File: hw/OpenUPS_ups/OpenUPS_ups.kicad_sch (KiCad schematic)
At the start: 15 parts, among them J101 XT60PW-M, J102 Barrel Jack, J103 Screw Terminal, J104 Screw Terminal, J105 Screw Terminal, J106 JST XH, J107 JST XH, U102 AVR32DB48x-xPT

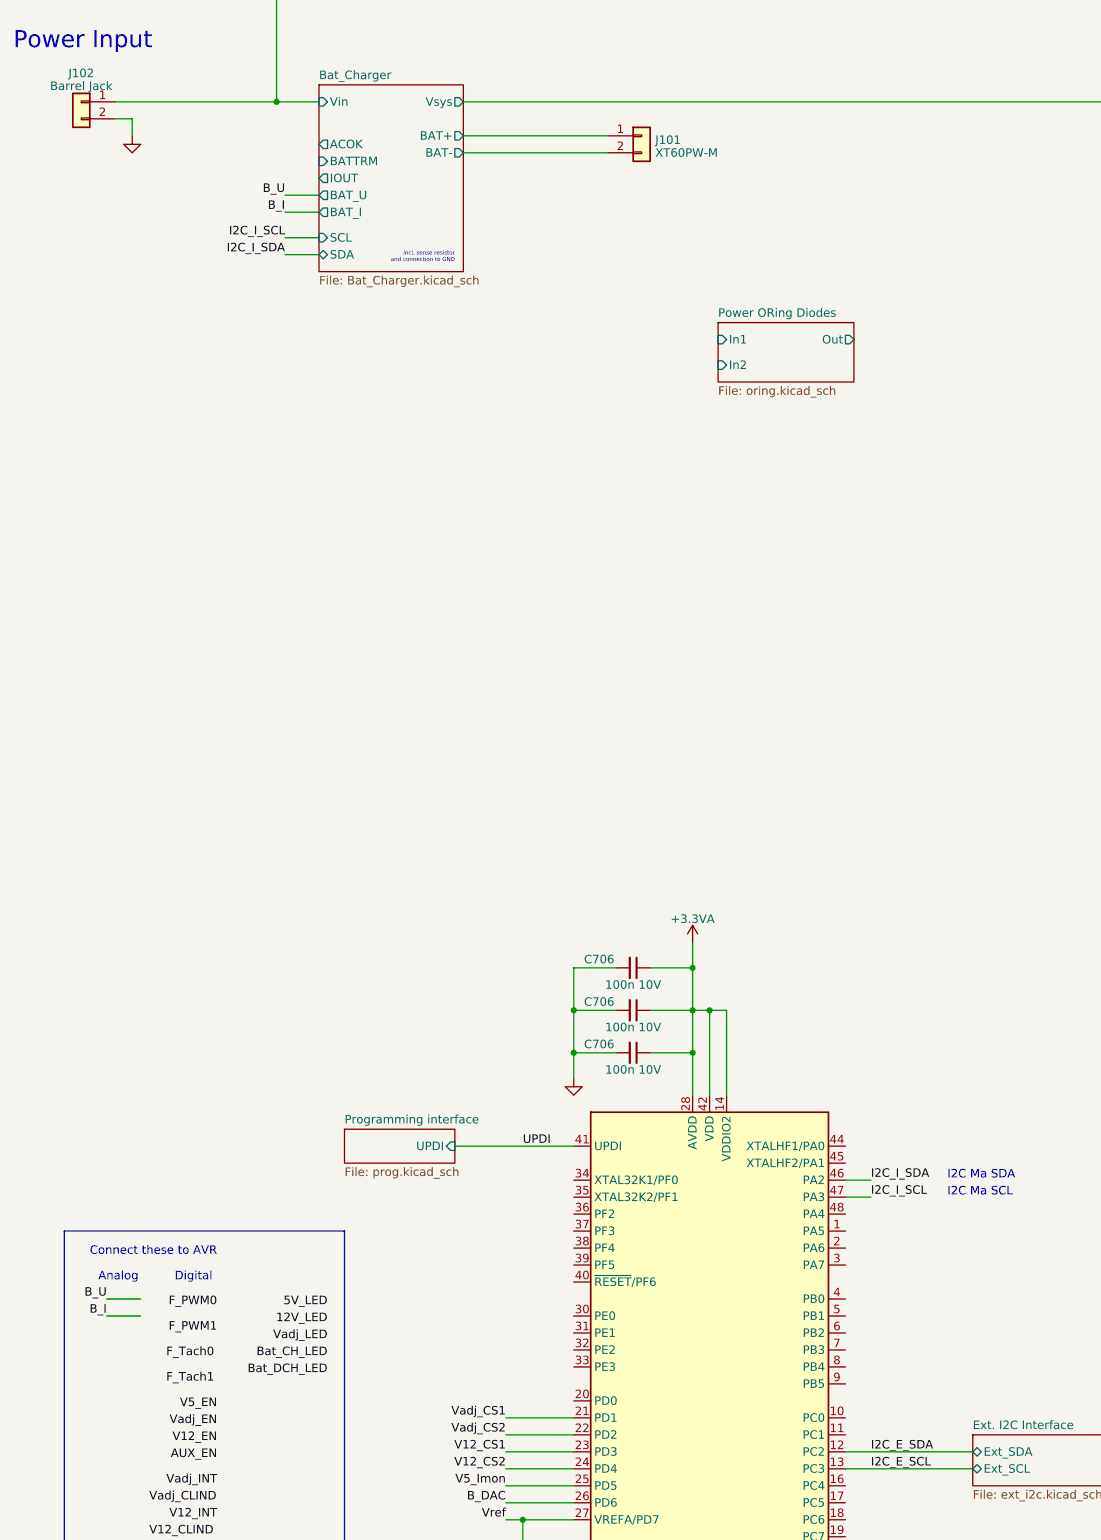
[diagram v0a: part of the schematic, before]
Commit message: Issue #24 - battery charger, good for review
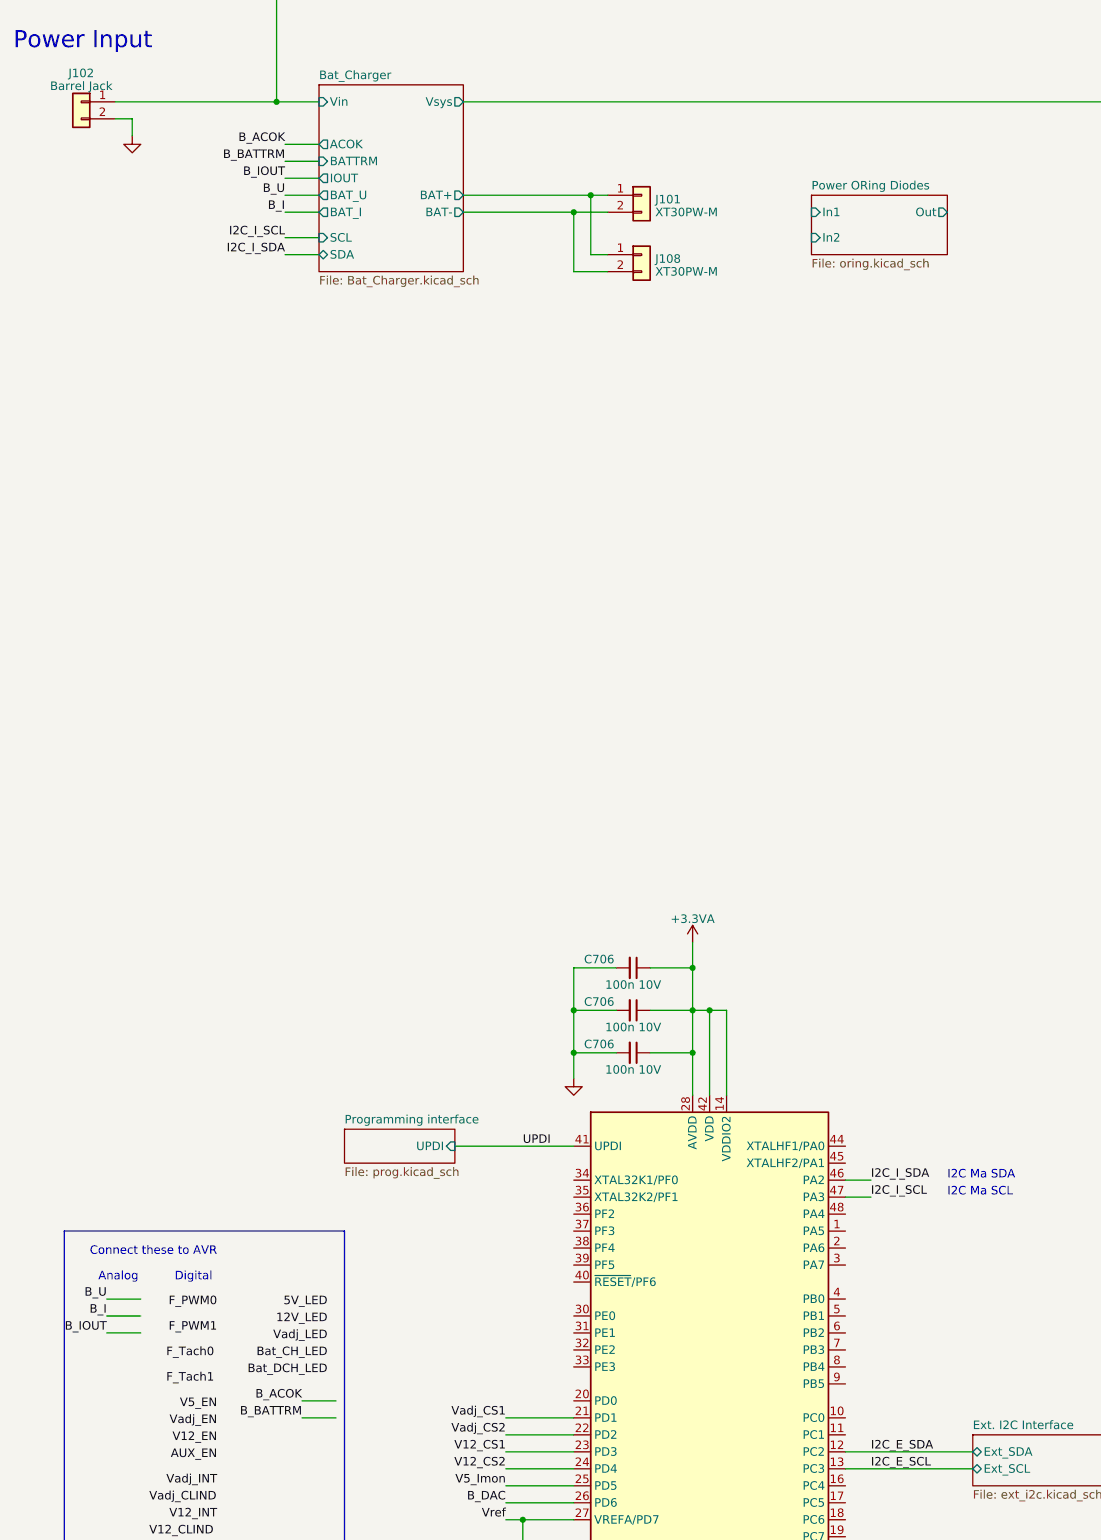
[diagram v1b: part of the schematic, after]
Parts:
- added J108: XT30PW-M, Connector_AMASS:AMASS_XT30PW-M_1x02_P2.50mm_Horizontal, symbol Connector_Generic:Conn_01x02
- J101: value XT60PW-M -> XT30PW-M; footprint Connector_AMASS:AMASS_XT60PW-M_1x02_P7.20mm_Horizontal -> Connector_AMASS:AMASS_XT30PW-M_1x02_P2.50mm_Horizontal
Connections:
- net Bat_Charger/BAT+: now also J108.1 (Pin_1)
- net Bat_Charger/BAT-: now also J108.2 (Pin_2)
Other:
- note removed: "incl. sense resistor and connection to GND"
- moved on the sheet: J101
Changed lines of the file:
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@@
   (junction (at 90.17 257.81) (diameter 0) (color 0 0 0 0)
+  )
+  (junction (at 100.33 59.69) (diameter 0) (color 0 0 0 0)
+  )
+  (junction (at 97.79 62.23) (diameter 0) (color 0 0 0 0)
   )
   (wire (pts (xy 87.63 255.27) (xy 97.79 255.27))
@@
     (stroke (width 0) (type default))
   )
-  (wire (pts (xy 81.28 50.8) (xy 102.87 50.8))
+  (wire (pts (xy 81.28 59.69) (xy 100.33 59.69))
     (stroke (width 0.5) (type default))
   )
+  (wire (pts (xy 97.79 62.23) (xy 102.87 62.23))
+    (stroke (width 0.5) (type default))
+  )
   (wire (pts (xy 203.2 49.53) (xy 208.28 49.53))
     (stroke (width 0) (type default))
@@
   )
   (wire (pts (xy 87.63 242.57) (xy 97.79 242.57))
+    (stroke (width 0) (type default))
+  )
+  (wire (pts (xy 54.61 52.07) (xy 59.69 52.07))
     (stroke (width 0) (type default))
   )
@@
     (stroke (width 0) (type default))
   )
+  (wire (pts (xy 27.94 229.87) (xy 33.02 229.87))
+    (stroke (width 0) (type default))
+  )
   (wire (pts (xy 302.26 68.58) (xy 302.26 69.85))
     (stroke (width 0) (type default))
@@
     (stroke (width 0) (type default))
   )
+  (wire (pts (xy 100.33 68.58) (xy 100.33 59.69))
+    (stroke (width 0.5) (type default))
+  )
   (wire (pts (xy 120.65 181.61) (xy 118.11 181.61))
     (stroke (width 0) (type default))
@@
     (stroke (width 0) (type default))
   )
+  (wire (pts (xy 57.15 240.03) (xy 62.23 240.03))
+    (stroke (width 0) (type default))
+  )
   (wire (pts (xy 27.94 224.79) (xy 33.02 224.79))
     (stroke (width 0) (type default))
   )
+  (wire (pts (xy 100.33 59.69) (xy 102.87 59.69))
+    (stroke (width 0.5) (type default))
+  )
+  (wire (pts (xy 97.79 71.12) (xy 97.79 62.23))
+    (stroke (width 0.5) (type default))
+  )
   (wire (pts (xy 208.28 20.32) (xy 187.96 20.32))
     (stroke (width 0) (type default))
@@
     (stroke (width 0) (type default))
   )
+  (wire (pts (xy 102.87 68.58) (xy 100.33 68.58))
+    (stroke (width 0.5) (type default))
+  )
   (wire (pts (xy 138.43 207.01) (xy 142.24 207.01))
     (stroke (width 0) (type default))
   )
-  (wire (pts (xy 81.28 53.34) (xy 102.87 53.34))
+  (wire (pts (xy 81.28 62.23) (xy 97.79 62.23))
     (stroke (width 0.5) (type default))
   )
@@
   )
   (wire (pts (xy 87.63 250.19) (xy 97.79 250.19))
+    (stroke (width 0) (type default))
+  )
+  (wire (pts (xy 54.61 57.15) (xy 59.69 57.15))
     (stroke (width 0) (type default))
   )
@@
     (stroke (width 0) (type default))
   )
+  (wire (pts (xy 57.15 242.57) (xy 62.23 242.57))
+    (stroke (width 0) (type default))
+  )
   (wire (pts (xy 234.95 49.53) (xy 229.87 49.53))
     (stroke (width 0) (type default))
@@
   (wire (pts (xy 203.2 85.09) (xy 208.28 85.09))
     (stroke (width 0) (type default))
+  )
+  (wire (pts (xy 102.87 71.12) (xy 97.79 71.12))
+    (stroke (width 0.5) (type default))
   )
   (wire (pts (xy 87.63 245.11) (xy 97.79 245.11))
@@
     (stroke (width 0.5) (type default))
   )
+  (wire (pts (xy 54.61 54.61) (xy 59.69 54.61))
+    (stroke (width 0) (type default))
+  )
   (wire (pts (xy 303.53 172.72) (xy 303.53 175.26))
     (stroke (width 0) (type default))
@@
     (effects (font (size 1.27 1.27)) (justify left bottom))
   )
-  (text "incl. sense resistor\nand connection to GND" (at 80.01 69.85 0)
-    (effects (font (size 0.6 0.6)) (justify right bottom))
-  )
   (text "Powered from +5V" (at 290.83 104.14 0)
     (effects (font (size 1.27 1.27)) (justify left bottom))
@@
     (effects (font (size 1.27 1.27)) (justify right bottom))
   )
+  (label "B_BATTRM" (at 57.15 242.57 180) (fields_autoplaced)
+    (effects (font (size 1.27 1.27)) (justify right bottom))
+  )
+  (label "B_BATTRM" (at 54.61 54.61 180) (fields_autoplaced)
+    (effects (font (size 1.27 1.27)) (justify right bottom))
+  )
   (label "Vadj_INT" (at 44.45 252.73 180) (fields_autoplaced)
     (effects (font (size 1.27 1.27)) (justify right bottom))
@@
     (effects (font (size 1.27 1.27)) (justify right bottom))
   )
+  (label "B_IOUT" (at 54.61 57.15 180) (fields_autoplaced)
+    (effects (font (size 1.27 1.27)) (justify right bottom))
+  )
   (label "V5_EN" (at 203.2 120.65 180) (fields_autoplaced)
     (effects (font (size 1.27 1.27)) (justify right bottom))
@@
     (effects (font (size 1.27 1.27)) (justify right bottom))
   )
+  (label "B_ACOK" (at 57.15 240.03 180) (fields_autoplaced)
+    (effects (font (size 1.27 1.27)) (justify right bottom))
+  )
   (label "5V_LED" (at 60.96 226.06 180) (fields_autoplaced)
     (effects (font (size 1.27 1.27)) (justify right bottom))
@@
   )
   (label "AUX_EN" (at 44.45 248.92 180) (fields_autoplaced)
+    (effects (font (size 1.27 1.27)) (justify right bottom))
+  )
+  (label "B_ACOK" (at 54.61 52.07 180) (fields_autoplaced)
+    (effects (font (size 1.27 1.27)) (justify right bottom))
+  )
+  (label "B_IOUT" (at 27.94 229.87 180) (fields_autoplaced)
     (effects (font (size 1.27 1.27)) (justify right bottom))
   )
@@
     )
   )
+  (symbol (lib_id "Connector_Generic:Conn_01x02") (at 107.95 68.58 0) (unit 1)
+    (in_bom yes) (on_board yes) (dnp no) (fields_autoplaced)
+    (property "Reference" "J108" (at 109.982 69.2063 0)
+      (effects (font (size 1.27 1.27)) (justify left))
+    )
+    (property "Value" "XT30PW-M" (at 109.982 71.1273 0)
+      (effects (font (size 1.27 1.27)) (justify left))
+    )
+    (property "Footprint" "Connector_AMASS:AMASS_XT30PW-M_1x02_P2.50mm_Horizontal" (at 107.95 68.58 0)
+      (effects (font (size 1.27 1.27)) hide)
+    )
+    (property "Datasheet" "~" (at 107.95 68.58 0)
+      (effects (font (size 1.27 1.27)) hide)
+    )
+    (pin "1")
+    (pin "2")
+    (instances
+      (project "OpenUPS_ups"
+        (path "/f77faec3-eac4-47f3-a2de-ec4a039f4502"
+          (reference "J108") (unit 1)
+        )
+      )
+    )
+  )
   (symbol (lib_id "power:GND") (at 302.26 88.9 0) (unit 1)
     (in_bom yes) (on_board yes) (dnp no)
@@
     )
   )
-  (symbol (lib_id "Connector_Generic:Conn_01x02") (at 107.95 50.8 0) (unit 1)
+  (symbol (lib_id "Connector_Generic:Conn_01x02") (at 107.95 59.69 0) (unit 1)
     (in_bom yes) (on_board yes) (dnp no) (fields_autoplaced)
-    (property "Reference" "J101" (at 109.982 51.4263 0)
-      (effects (font (size 1.27 1.27)) (justify left))
-    )
-    (property "Value" "XT60PW-M" (at 109.982 53.3473 0)
-      (effects (font (size 1.27 1.27)) (justify left))
-    )
-    (property "Footprint" "Connector_AMASS:AMASS_XT60PW-M_1x02_P7.20mm_Horizontal" (at 107.95 50.8 0)
-      (effects (font (size 1.27 1.27)) hide)
-    )
-    (property "Datasheet" "~" (at 107.95 50.8 0)
+    (property "Reference" "J101" (at 109.982 60.3163 0)
+      (effects (font (size 1.27 1.27)) (justify left))
+    )
+    (property "Value" "XT30PW-M" (at 109.982 62.2373 0)
+      (effects (font (size 1.27 1.27)) (justify left))
+    )
+    (property "Footprint" "Connector_AMASS:AMASS_XT30PW-M_1x02_P2.50mm_Horizontal" (at 107.95 59.69 0)
+      (effects (font (size 1.27 1.27)) hide)
+    )
+    (property "Datasheet" "~" (at 107.95 59.69 0)
       (effects (font (size 1.27 1.27)) hide)
     )
@@
       (effects (font (size 1.27 1.27)) (justify left top))
     )
-    (pin "BAT+" output (at 81.28 50.8 0)
+    (pin "BAT+" output (at 81.28 59.69 0)
       (effects (font (size 1.27 1.27)) (justify right))
     )
-    (pin "BAT-" output (at 81.28 53.34 0)
+    (pin "BAT-" output (at 81.28 62.23 0)
       (effects (font (size 1.27 1.27)) (justify right))
     )
@@
     )
   )
-  (sheet (at 119.38 78.74) (size 20.32 8.89) (fields_autoplaced)
+  (sheet (at 133.35 59.69) (size 20.32 8.89) (fields_autoplaced)
     (stroke (width 0.1524) (type solid))
     (fill (color 0 0 0 0.0000))
-    (property "Sheetname" "Power ORing Diodes" (at 119.38 78.0284 0)
+    (property "Sheetname" "Power ORing Diodes" (at 133.35 58.9784 0)
       (effects (font (size 1.27 1.27)) (justify left bottom))
     )
-    (property "Sheetfile" "oring.kicad_sch" (at 119.38 88.2146 0)
+    (property "Sheetfile" "oring.kicad_sch" (at 133.35 69.1646 0)
       (effects (font (size 1.27 1.27)) (justify left top))
     )
-    (pin "In1" input (at 119.38 81.28 180)
-      (effects (font (size 1.27 1.27)) (justify left))
-    )
-    (pin "Out" output (at 139.7 81.28 0)
+    (pin "In1" input (at 133.35 62.23 180)
+      (effects (font (size 1.27 1.27)) (justify left))
+    )
+    (pin "Out" output (at 153.67 62.23 0)
       (effects (font (size 1.27 1.27)) (justify right))
     )
-    (pin "In2" input (at 119.38 85.09 180)
-      (effects (font (size 1.27 1.27)) (justify left))
-    )
+    (pin "In2" input (at 133.35 66.04 180)
+      (effects (font (size 1.27 1.27)) (justify left))
+    )
